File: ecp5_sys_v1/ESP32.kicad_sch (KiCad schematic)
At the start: 0 parts

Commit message: Worked on USB
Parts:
- added U3: ESP32-S3-WROOM-1, RF_Module:ESP32-S3-WROOM-1, symbol RF_Module:ESP32-S3-WROOM-1
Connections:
- new net: U3.1 (GND), U3.40 (GND), U3.41 (GND)
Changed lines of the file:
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@@
 	(generator_version "10.0")
 	(paper "A4")
+	(symbol
+		(lib_id "RF_Module:ESP32-S3-WROOM-1")
+		(at 129.54 74.93 0)
+		(unit 1)
+		(body_style 1)
+		(exclude_from_sim no)
+		(in_bom yes)
+		(on_board yes)
+		(in_pos_files yes)
+		(dnp no)
+		(fields_autoplaced yes)
+		(property "Reference" "U3"
+			(at 131.6833 44.45 0)
+			(show_name no)
+			(do_not_autoplace no)
+			(effects
+				(font
+					(size 1.27 1.27)
+				)
+				(justify left)
+			)
+		)
+		(property "Value" "ESP32-S3-WROOM-1"
+			(at 131.6833 46.99 0)
+			(show_name no)
+			(do_not_autoplace no)
+			(effects
+				(font
+					(size 1.27 1.27)
+				)
+				(justify left)
+			)
+		)
+		(property "Footprint" "RF_Module:ESP32-S3-WROOM-1"
+			(at 129.54 72.39 0)
+			(hide yes)
+			(show_name no)
+			(do_not_autoplace no)
+			(effects
+				(font
+					(size 1.27 1.27)
+				)
+			)
+		)
+		(property "Datasheet" "https://www.espressif.com/sites/default/files/documentation/esp32-s3-wroom-1_wroom-1u_datasheet_en.pdf"
+			(at 129.54 74.93 0)
+			(hide yes)
+			(show_name no)
+			(do_not_autoplace no)
+			(effects
+				(font
+					(size 1.27 1.27)
+				)
+			)
+		)
+		(property "Description" "RF Module, ESP32-S3 SoC, Wi-Fi 802.11b/g/n, Bluetooth, BLE, 32-bit, 3.3V, onboard antenna, SMD"
+			(at 129.54 74.93 0)
+			(hide yes)
+			(show_name no)
+			(do_not_autoplace no)
+			(effects
+				(font
+					(size 1.27 1.27)
+				)
+			)
+		)
+		(pin "40"
+		)
+		(pin "41"
+		)
+		(pin "38"
+		)
+		(pin "36"
+		)
+		(pin "33"
+		)
+		(pin "34"
+		)
+		(pin "35"
+		)
+		(pin "37"
+		)
+		(pin "39"
+		)
+		(pin "16"
+		)
+		(pin "30"
+		)
+		(pin "26"
+		)
+		(pin "32"
+		)
+		(pin "29"
+		)
+		(pin "31"
+		)
+		(pin "4"
+		)
+		(pin "10"
+		)
+		(pin "19"
+		)
+		(pin "13"
+		)
+		(pin "20"
+		)
+		(pin "21"
+		)
+		(pin "27"
+		)
+		(pin "6"
+		)
+		(pin "11"
+		)
+		(pin "2"
+		)
+		(pin "7"
+		)
+		(pin "3"
+		)
+		(pin "9"
+		)
+		(pin "12"
+		)
+		(pin "8"
+		)
+		(pin "14"
+		)
+		(pin "1"
+		)
+		(pin "5"
+		)
+		(pin "15"
+		)
+		(pin "17"
+		)
+		(pin "18"
+		)
+		(pin "22"
+		)
+		(pin "23"
+		)
+		(pin "24"
+		)
+		(pin "25"
+		)
+		(pin "28"
+		)
+		(instances
+			(project "ecp5_sys_v1"
+				(path "/08f8cf6b-931b-453e-b2e0-0373288a9134/d04e611c-2826-4bf8-b2d8-77f691cf1818"
+					(reference "U3")
+					(unit 1)
+				)
+			)
+		)
+	)
 )

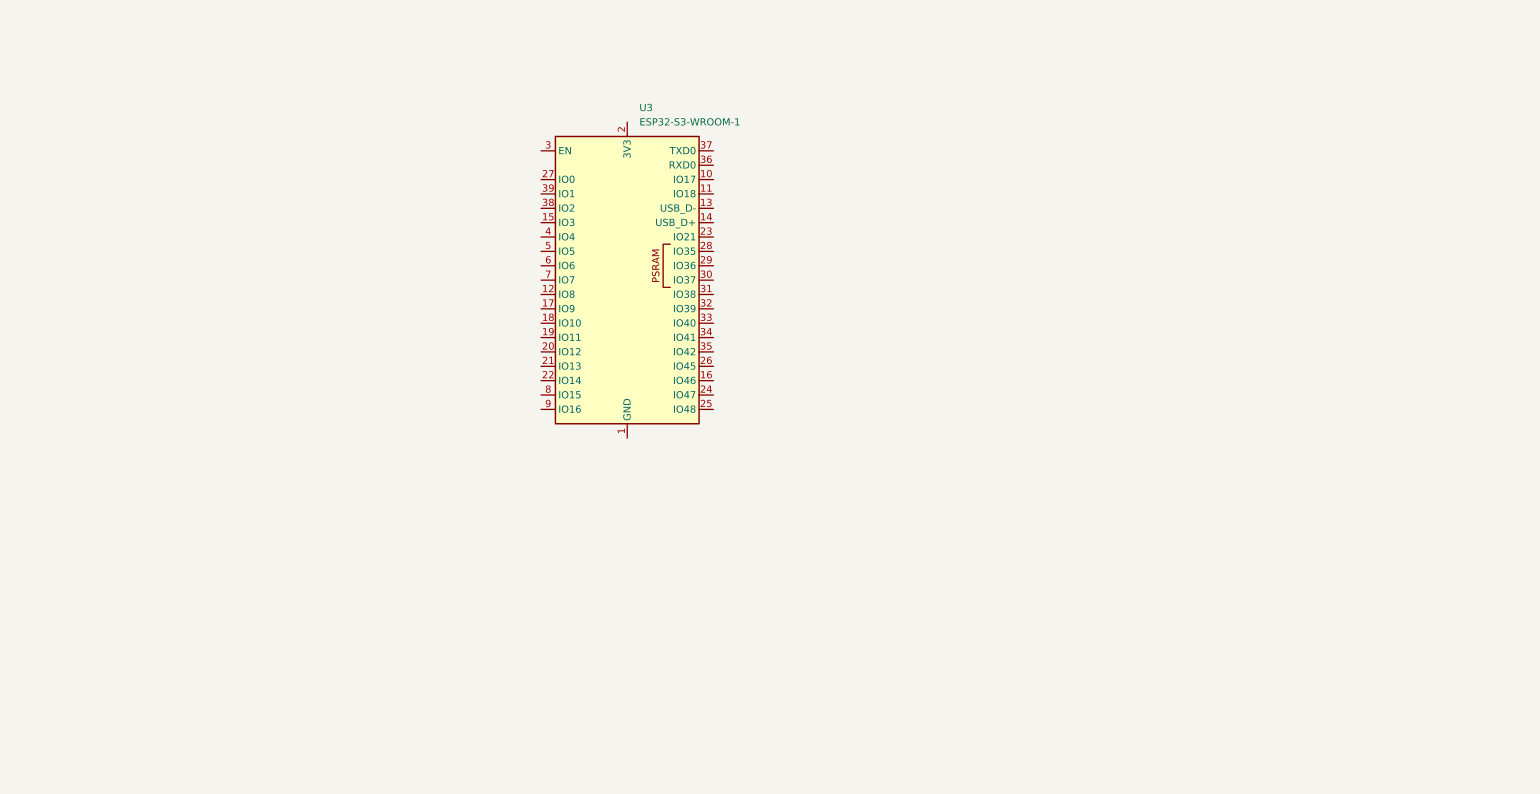
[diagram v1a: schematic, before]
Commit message: Finished USB schematic, left pins for future work and worked on ESP32, FPGA config, things have been confirmed, next up is thinking about power and how it will function into if the system is going to be just a DVP camera or also MIPI
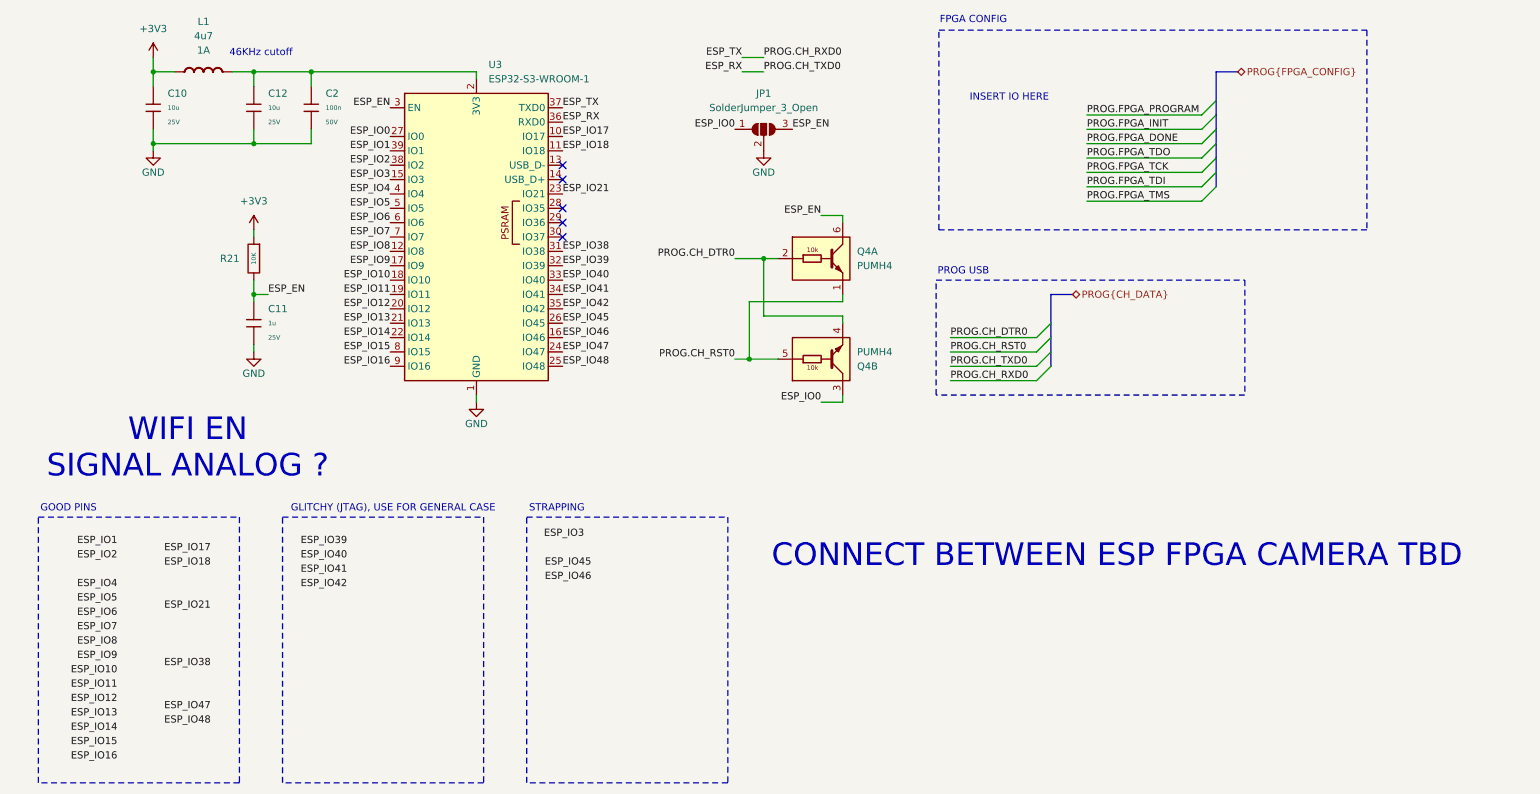
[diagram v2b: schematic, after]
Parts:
- added C10, C12: 10u, PCM_JLCPCB:C_0603, symbol PCM_JLCPCB-Capacitors:0603,10uF,(2)
- added C11: 1u, PCM_JLCPCB:C_0402, symbol PCM_JLCPCB-Capacitors:0402,1uF
- added C2: 100n, PCM_JLCPCB:C_0402, symbol PCM_JLCPCB-Capacitors:0402,100nF,(2)
- added JP1: SolderJumper_3_Open, Jumper:SolderJumper-3_P1.3mm_Open_RoundedPad1.0x1.5mm, symbol Jumper:SolderJumper_3_Open
- added L1: 4u7, Inductor_SMD:L_1008_2520Metric, symbol PCM_Elektuur:L
- added Q4: PUMH4, PCM_Package_TO_SOT_SMD_AKL:SOT-363_SC-70-6, symbol PCM_Transistor_BJT_Pre-Biased_AKL:PUMH4
- added R21: 10K, PCM_JLCPCB:R_0402, symbol PCM_JLCPCB-Resistors:0402,10kΩ
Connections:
- net GND: now reaches U3.1 (GND), U3.40 (GND), U3.41 (GND)
- net GND: now also C10.2, C11.2, C12.2, C2.2, JP1.2 (C)
- net ESP_IO17: now reaches U3.10 (IO17)
- net ESP_IO18: now reaches U3.11 (IO18)
- net ESP_IO8: now reaches U3.12 (IO8)
- net ESP_IO3: now reaches U3.15 (IO3)
- net ESP_IO46: now reaches U3.16 (IO46)
- net ESP_IO9: now reaches U3.17 (IO9)
- net ESP_IO10: now reaches U3.18 (IO10)
- net ESP_IO11: now reaches U3.19 (IO11)
- net at U3.2 (3V3): now also C12.1, C2.1, L1.2 (-)
- net ESP_IO12: now reaches U3.20 (IO12)
- net ESP_IO13: now reaches U3.21 (IO13)
- net ESP_IO14: now reaches U3.22 (IO14)
- net ESP_IO21: now reaches U3.23 (IO21)
- net ESP_IO47: now reaches U3.24 (IO47)
- net ESP_IO48: now reaches U3.25 (IO48)
- net ESP_IO45: now reaches U3.26 (IO45)
- net ESP_IO0: now reaches U3.27 (IO0)
- net ESP_IO0: now also JP1.1 (A), Q4.3 (C2)
- net ESP_EN: now reaches U3.3 (EN)
- net ESP_EN: now also C11.1, JP1.3 (B), Q4.6 (C1), R21.2
- net ESP_IO38: now reaches U3.31 (IO38)
- net ESP_IO39: now reaches U3.32 (IO39)
- net ESP_IO40: now reaches U3.33 (IO40)
- net ESP_IO41: now reaches U3.34 (IO41)
- net ESP_IO42: now reaches U3.35 (IO42)
- net ESP_RX: now reaches U3.36 (RXD0)
- net ESP_TX: now reaches U3.37 (TXD0)
- net ESP_IO2: now reaches U3.38 (IO2)
- net ESP_IO1: now reaches U3.39 (IO1)
- net ESP_IO4: now reaches U3.4 (IO4)
- net ESP_IO5: now reaches U3.5 (IO5)
- net ESP_IO6: now reaches U3.6 (IO6)
- net ESP_IO7: now reaches U3.7 (IO7)
- net ESP_IO15: now reaches U3.8 (IO15)
- net ESP_IO16: now reaches U3.9 (IO16)
- new net +3V3: C10.1, L1.1 (+), R21.1
- new net PROG.CH_DTR0: Q4.2 (B1), Q4.4 (E2)
- new net PROG.CH_RST0: Q4.1 (E1), Q4.5 (B2)
- no-connect marks 0 -> 5
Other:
- note added: "46KHz cutoff"
- note added: "CONNECT BETWEEN ESP FPGA CAMERA TBD"
- note added: "FPGA CONFIG"
- note added: "GLITCHY (JTAG), USE FOR GENERAL CASE"
- note added: "GOOD PINS"
- note added: "INSERT IO HERE"
- note added: "PROG USB"
- note added: "STRAPPING"
- note added: "WIFI EN SIGNAL ANALOG ?"
- moved on the sheet: U3

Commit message: worked on power, should have external IC for sequencing and FPGA power is fine, started work in the CAMERA FPC, power 2V8 and 1V2 are there as LDOs, small package, should be fine.
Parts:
- renumbered C10 to C2, C12 to C3, C11 to C4, C2 to C5, Q4 to Q1, R21 to R7
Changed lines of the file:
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@@
 		(dnp no)
 		(fields_autoplaced yes)
-		(property "Reference" "R21"
+		(property "Reference" "R7"
 			(at 60.96 71.1199 0)
 			(show_name no)
@@
 			(project "ecp5_sys_v1"
 				(path "/08f8cf6b-931b-453e-b2e0-0373288a9134/d04e611c-2826-4bf8-b2d8-77f691cf1818"
-					(reference "R21")
+					(reference "R7")
 					(unit 1)
 				)
@@
 		(dnp no)
 		(fields_autoplaced yes)
-		(property "Reference" "C11"
+		(property "Reference" "C4"
 			(at 66.04 80.0099 0)
 			(show_name no)
@@
 			(project "ecp5_sys_v1"
 				(path "/08f8cf6b-931b-453e-b2e0-0373288a9134/d04e611c-2826-4bf8-b2d8-77f691cf1818"
-					(reference "C11")
+					(reference "C4")
 					(unit 1)
 				)
@@
 		(dnp no)
 		(fields_autoplaced yes)
-		(property "Reference" "C2"
+		(property "Reference" "C5"
 			(at 76.2 41.9099 0)
 			(show_name no)
@@
 			(project "ecp5_sys_v1"
 				(path "/08f8cf6b-931b-453e-b2e0-0373288a9134/d04e611c-2826-4bf8-b2d8-77f691cf1818"
-					(reference "C2")
+					(reference "C5")
 					(unit 1)
 				)
@@
 		(dnp no)
 		(fields_autoplaced yes)
-		(property "Reference" "#PWR031"
+		(property "Reference" "#PWR011"
 			(at 45.72 39.37 0)
 			(hide yes)
@@
 			(project "ecp5_sys_v1"
 				(path "/08f8cf6b-931b-453e-b2e0-0373288a9134/d04e611c-2826-4bf8-b2d8-77f691cf1818"
-					(reference "#PWR031")
+					(reference "#PWR011")
 					(unit 1)
 				)
@@
 		(in_pos_files yes)
 		(dnp no)
-		(property "Reference" "Q4"
+		(property "Reference" "Q1"
 			(at 170.18 90.1701 0)
 			(show_name no)
@@
 			(project "ecp5_sys_v1"
 				(path "/08f8cf6b-931b-453e-b2e0-0373288a9134/d04e611c-2826-4bf8-b2d8-77f691cf1818"
-					(reference "Q4")
+					(reference "Q1")
 					(unit 2)
 				)
@@
 		(dnp no)
 		(fields_autoplaced yes)
-		(property "Reference" "#PWR014"
+		(property "Reference" "#PWR012"
 			(at 45.72 58.42 0)
 			(hide yes)
@@
 			(project "ecp5_sys_v1"
 				(path "/08f8cf6b-931b-453e-b2e0-0373288a9134/d04e611c-2826-4bf8-b2d8-77f691cf1818"
-					(reference "#PWR014")
+					(reference "#PWR012")
 					(unit 1)
 				)
@@
 		(dnp no)
 		(fields_autoplaced yes)
-		(property "Reference" "#PWR021"
+		(property "Reference" "#PWR014"
 			(at 63.5 93.98 0)
 			(hide yes)
@@
 			(project "ecp5_sys_v1"
 				(path "/08f8cf6b-931b-453e-b2e0-0373288a9134/d04e611c-2826-4bf8-b2d8-77f691cf1818"
-					(reference "#PWR021")
+					(reference "#PWR014")
 					(unit 1)
 				)
@@
 		(dnp no)
 		(fields_autoplaced yes)
-		(property "Reference" "#PWR012"
+		(property "Reference" "#PWR015"
 			(at 102.87 102.87 0)
 			(hide yes)
@@
 			(project "ecp5_sys_v1"
 				(path "/08f8cf6b-931b-453e-b2e0-0373288a9134/d04e611c-2826-4bf8-b2d8-77f691cf1818"
-					(reference "#PWR012")
+					(reference "#PWR015")
 					(unit 1)
 				)
@@
 		(dnp no)
 		(fields_autoplaced yes)
-		(property "Reference" "Q4"
+		(property "Reference" "Q1"
 			(at 170.18 69.8499 0)
 			(show_name no)
@@
 			(project "ecp5_sys_v1"
 				(path "/08f8cf6b-931b-453e-b2e0-0373288a9134/d04e611c-2826-4bf8-b2d8-77f691cf1818"
-					(reference "Q4")
+					(reference "Q1")
 					(unit 1)
 				)
@@
 		(dnp no)
 		(fields_autoplaced yes)
-		(property "Reference" "C10"
+		(property "Reference" "C2"
 			(at 48.26 41.9099 0)
 			(show_name no)
@@
 			(project "ecp5_sys_v1"
 				(path "/08f8cf6b-931b-453e-b2e0-0373288a9134/d04e611c-2826-4bf8-b2d8-77f691cf1818"
-					(reference "C10")
+					(reference "C2")
 					(unit 1)
 				)
@@
 		(dnp no)
 		(fields_autoplaced yes)
-		(property "Reference" "#PWR015"
+		(property "Reference" "#PWR013"
 			(at 63.5 69.85 0)
 			(hide yes)
@@
 			(project "ecp5_sys_v1"
 				(path "/08f8cf6b-931b-453e-b2e0-0373288a9134/d04e611c-2826-4bf8-b2d8-77f691cf1818"
-					(reference "#PWR015")
+					(reference "#PWR013")
 					(unit 1)
 				)
@@
 		(dnp no)
 		(fields_autoplaced yes)
-		(property "Reference" "C12"
+		(property "Reference" "C3"
 			(at 66.04 41.9099 0)
 			(show_name no)
@@
 			(project "ecp5_sys_v1"
 				(path "/08f8cf6b-931b-453e-b2e0-0373288a9134/d04e611c-2826-4bf8-b2d8-77f691cf1818"
-					(reference "C12")
+					(reference "C3")
 					(unit 1)
 				)
@@
 		(dnp no)
 		(fields_autoplaced yes)
-		(property "Reference" "#PWR030"
+		(property "Reference" "#PWR016"
 			(at 153.67 58.42 0)
 			(hide yes)
@@
 			(project "ecp5_sys_v1"
 				(path "/08f8cf6b-931b-453e-b2e0-0373288a9134/d04e611c-2826-4bf8-b2d8-77f691cf1818"
-					(reference "#PWR030")
+					(reference "#PWR016")
 					(unit 1)
 				)
